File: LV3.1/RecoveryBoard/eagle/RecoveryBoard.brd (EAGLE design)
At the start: 120.9 x 54.6 mm, 96 parts, among them Q1 BSS123, Q2 BSS123, Q3 BSS123, Q4 BPR-301, Q5 BPR-301, Q6 MOSFET-PCH-SOT23-6, U1 STM32F042K6, U10 TPS63070, U2 BD62120AEFJ-E2, Y1 ECS-160-10-36Q-ES-TR

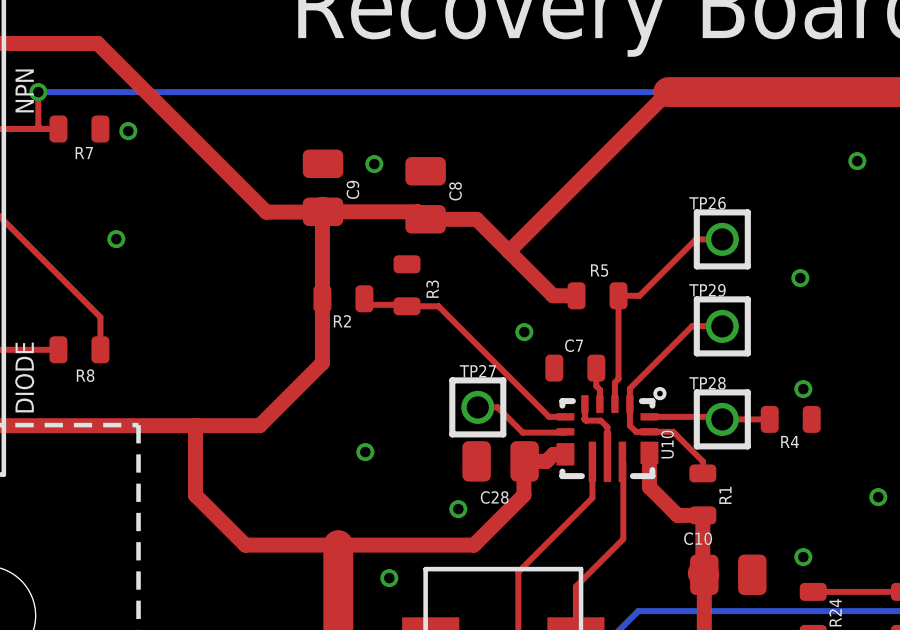
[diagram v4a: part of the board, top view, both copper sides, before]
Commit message: finished bom without jtag and connectors
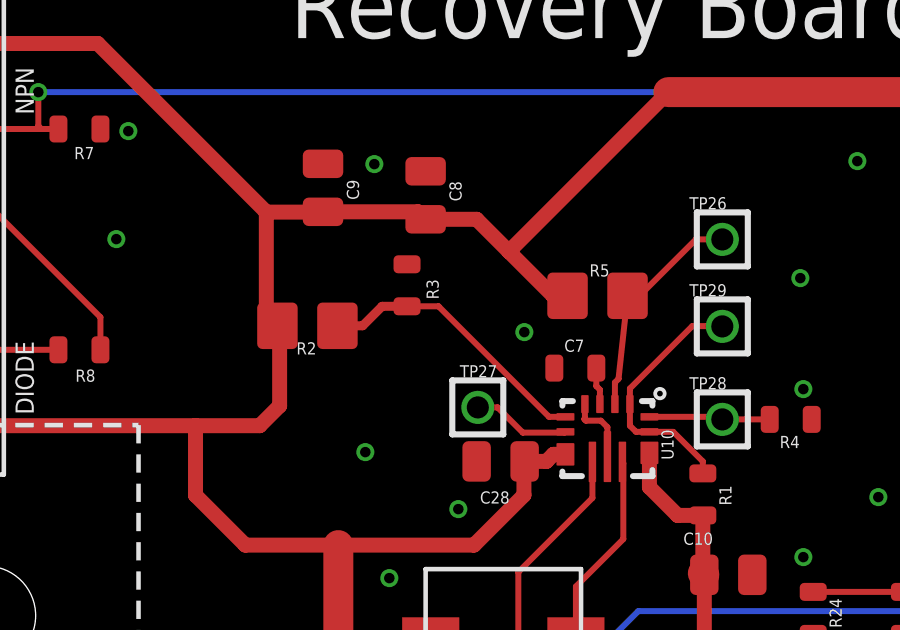
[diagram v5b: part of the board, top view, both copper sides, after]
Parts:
- R2, R5: device oresat-rcl:.0603-C-NOSILK -> oresat-rcl:.0805-A-NOSILK
- moved R2 1.50 mm to (20.9, 41.4)
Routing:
- net TPS-FB: track 8.33 -> 9.40 mm
- net 3.3V: track 312.0 -> 311.3 mm
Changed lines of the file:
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@@
 <drawing>
 <settings>
-<setting alwaysvectorfont="yes"/>
+<setting alwaysvectorfont="no"/>
 <setting verticaltext="up"/>
 </settings>
@@
 <attribute name="VALUE" x="58.22" y="43.13" size="0.4064" layer="27" font="vector" ratio="15" rot="R270"/>
 </element>
-<element name="R2" library="oresat-rcl" package=".0603-C-NOSILK" value="470k" x="22.07" y="42.31" smashed="yes" rot="R180">
-<attribute name="DIS" value="Digi-Key" x="-30" y="102" size="1.778" layer="27" rot="R180" display="off"/>
-<attribute name="DPN" value="1276-4275-1-ND" x="-30" y="102" size="1.778" layer="27" rot="R180" display="off"/>
-<attribute name="MFR" value="Samsung" x="-30" y="102" size="1.778" layer="27" rot="R180" display="off"/>
-<attribute name="MPN" value="RC1005F6653CS" x="-30" y="102" size="1.778" layer="27" rot="R180" display="off"/>
-<attribute name="NAME" x="22.37" y="41.76" size="0.4064" layer="25" font="vector" ratio="15" rot="R180"/>
-<attribute name="NAME" x="22.07" y="42.31" size="0.2" layer="33" ratio="15" rot="R180" align="center"/>
-<attribute name="VALUE" x="22.87" y="43.66" size="0.4064" layer="27" font="vector" ratio="15" rot="R180"/>
+<element name="R2" library="oresat-rcl" package=".0805-A-NOSILK" value="470k" x="20.87" y="41.41" smashed="yes" rot="R180">
+<attribute name="DIS" value="Digi-Key" x="-31.2" y="101.1" size="1.778" layer="27" rot="R180" display="off"/>
+<attribute name="DPN" value="1276-4275-1-ND" x="-31.2" y="101.1" size="1.778" layer="27" rot="R180" display="off"/>
+<attribute name="MFR" value="Samsung" x="-31.2" y="101.1" size="1.778" layer="27" rot="R180" display="off"/>
+<attribute name="MPN" value="RC1005F6653CS" x="-31.2" y="101.1" size="1.778" layer="27" rot="R180" display="off"/>
+<attribute name="NAME" x="21.17" y="40.86" size="0.4064" layer="25" font="vector" ratio="15" rot="R180"/>
+<attribute name="NAME" x="20.87" y="41.41" size="0.2" layer="33" ratio="15" rot="R180" align="center"/>
+<attribute name="VALUE" x="21.67" y="42.76" size="0.4064" layer="27" font="vector" ratio="15" rot="R180"/>
 </element>
 <element name="R21" library="oresat-rcl" package=".0603-C-NOSILK" value="750" x="55.73" y="30.78" smashed="yes" rot="R90">
@@
 <attribute name="VALUE" x="37.78" y="39.64" size="0.4064" layer="27" font="vector" ratio="15" rot="R180"/>
 </element>
-<element name="R5" library="oresat-rcl" package=".0603-C-NOSILK" value="100k" x="30.54" y="42.41" smashed="yes" rot="R180">
+<element name="R5" library="oresat-rcl" package=".0805-A-NOSILK" value="100k" x="30.54" y="42.41" smashed="yes" rot="R180">
 <attribute name="DIS" value="Digi-Key" x="-35.5" y="102.1" size="1.778" layer="27" rot="R180" display="off"/>
 <attribute name="DPN" value="1276-4275-1-ND" x="-35.5" y="102.1" size="1.778" layer="27" rot="R180" display="off"/>
@@
 <wire x1="98.4" y1="9.6" x2="98.4" y2="4.545" width="1" layer="1"/>
 <wire x1="98.4" y1="4.545" x2="98.38" y2="4.525" width="1" layer="1"/>
-<wire x1="29.84" y1="42.41" x2="29.06" y2="42.41" width="0.5" layer="1"/>
+<wire x1="29.54" y1="42.41" x2="29.06" y2="42.41" width="0.5" layer="1"/>
 <wire x1="29.06" y1="42.41" x2="27.585" y2="43.885" width="0.5" layer="1"/>
 <wire x1="27.585" y1="43.885" x2="26.51" y2="44.96" width="0.5" layer="1"/>
@@
 <wire x1="21.39" y1="45.21" x2="24.56" y2="45.21" width="0.5" layer="1"/>
 <wire x1="24.56" y1="45.21" x2="24.81" y2="44.96" width="0.5" layer="1"/>
-<wire x1="21.37" y1="42.31" x2="21.37" y2="45.19" width="0.5" layer="1"/>
-<wire x1="21.37" y1="45.19" x2="21.39" y2="45.21" width="1" layer="1"/>
 <wire x1="27.585" y1="43.885" x2="32.9" y2="49.2" width="0.5" layer="1"/>
 <wire x1="56.02" y1="46.09" x2="52.91" y2="49.2" width="1" layer="1"/>
@@
 <wire x1="57.73" y1="44.38" x2="56.02" y2="46.09" width="0.5" layer="1"/>
 <wire x1="19.5" y1="45.2" x2="13.88" y2="50.82" width="0.5" layer="1"/>
-<wire x1="19.5" y1="45.2" x2="21.38" y2="45.2" width="0.5" layer="1"/>
+<wire x1="21.38" y1="45.2" x2="19.5" y2="45.2" width="0.5" layer="1"/>
 <wire x1="21.38" y1="45.2" x2="21.39" y2="45.21" width="0.5" layer="1"/>
-<wire x1="21.37" y1="42.31" x2="21.37" y2="40.17" width="0.5" layer="1"/>
 <wire x1="19.28" y1="38.08" x2="17.14" y2="38.08" width="0.5" layer="1"/>
-<wire x1="21.37" y1="40.17" x2="19.28" y2="38.08" width="0.5" layer="1"/>
+<wire x1="19.28" y1="38.08" x2="19.94376875" y2="38.74376875" width="0.5" layer="1"/>
 <wire x1="95.52" y1="32.95" x2="95.5" y2="32.93" width="0.5" layer="1"/>
 <wire x1="95.5" y1="32.93" x2="95.5" y2="32" width="0.5" layer="1"/>
@@
 <wire x1="111.154" y1="38.08" x2="106.78" y2="38.08" width="0.5" layer="1"/>
 <wire x1="106.78" y1="38.08" x2="103.7" y2="35" width="0.5" layer="1"/>
+<wire x1="19.5" y1="45.2" x2="19.5" y2="41.78" width="0.5" layer="1"/>
+<wire x1="19.5" y1="41.78" x2="19.87" y2="41.41" width="0.5" layer="1"/>
+<wire x1="19.94376875" y1="38.74376875" x2="19.94376875" y2="41.33623125" width="0.5" layer="1"/>
+<wire x1="19.94376875" y1="41.33623125" x2="19.87" y2="41.41" width="0.5" layer="1"/>
 </signal>
 <signal name="TPS-EN">
@@
 <wire x1="25.24" y1="42.06" x2="24.19" y2="42.06" width="0.2" layer="1"/>
 <wire x1="28.925" y1="38.375" x2="25.24" y2="42.06" width="0.2" layer="1"/>
-<wire x1="24.14" y1="42.11" x2="22.97" y2="42.11" width="0.2" layer="1"/>
-<wire x1="22.77" y1="42.31" x2="22.97" y2="42.11" width="0.2" layer="1"/>
-<wire x1="24.14" y1="42.11" x2="24.19" y2="42.06" width="0.2" layer="1"/>
+<wire x1="21.87" y1="41.41" x2="22.71" y2="41.41" width="0.3" layer="1"/>
+<wire x1="23.36" y1="42.06" x2="24.19" y2="42.06" width="0.3" layer="1"/>
+<wire x1="22.71" y1="41.41" x2="23.36" y2="42.06" width="0.3" layer="1"/>
 </signal>
 <signal name="TPS-PG">
@@
 <contactref element="R5" pad="1"/>
 <wire x1="33.82" y1="44.29" x2="31.94" y2="42.41" width="0.2" layer="1"/>
-<wire x1="31.24" y1="42.41" x2="31.94" y2="42.41" width="0.2" layer="1"/>
+<wire x1="31.54" y1="42.41" x2="31.94" y2="42.41" width="0.2" layer="1"/>
 <wire x1="33.82" y1="44.29" x2="34.7" y2="44.29" width="0.2" layer="1"/>
 <wire x1="31.12" y1="38.8" x2="31.12" y2="39.52" width="0.2" layer="1"/>
-<wire x1="31.24" y1="39.64" x2="31.24" y2="42.41" width="0.2" layer="1"/>
+<wire x1="31.24" y1="39.64" x2="31.54" y2="42.41" width="0.2" layer="1"/>
 <wire x1="31.12" y1="39.52" x2="31.24" y2="39.64" width="0.2" layer="1"/>
 </signal>
